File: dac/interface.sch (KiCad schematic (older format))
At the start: 14 parts, among them U17 DS90LV048, U18 74AUP1G74, U19 74AUP1G74

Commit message: DAC board is routed.  I also changed the digital interface to use a buffer (like I did on the input board) so that everything is buffered and we don't have multi-drop nets.
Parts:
- removed C73, C74: 220pF, Capacitor_SMD:C_0603_1608Metric, symbol Device:C_Small
- removed R65, R66: 68, Resistor_SMD:R_0603_1608Metric, symbol Device:R_US
- added C6, C7: 100nF, Capacitor_SMD:C_0603_1608Metric, symbol Device:C_Small
- added RN1, RN2, RN3: 33, Resistor_SMD:R_Array_Convex_4x0603, symbol Device:R_Pack04
- added U2: 74LVC541A, input:my-SSOP-20_5.3x7.2mm_P0.65mm, symbol 74xx:74LS541
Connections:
- net BCK: now also U2.3 (A1), U2.7 (A5)
- net DATA1: now also RN3.7 (R2.2); no longer U17.14 (RO2)
- net DATA2: now also RN3.8 (R1.2); no longer U17.15 (RO1)
- net GND: now also C6.2, C7.2, U2.1 (G1), U2.10 (GND), U2.19 (G2)
- net VCC: now also C6.1, C7.1, U2.20 (VCC)
- net U18FB: now reaches U18.2 (D), U18.3 (~Q)
- net U18Q: now reaches U18.5 (Q), U19.1 (C)
- net U19FB: now reaches U19.2 (D), U19.3 (~Q)
- net DOUT1+ renamed BCK+
- net DOUT1- renamed BCK-
- net DOUT2+ renamed DATA1+
- net DOUT2- renamed DATA1-
- net DOUT3+ renamed DATA2+
- net DOUT3- renamed DATA2-
- net SCK renamed SCK_DRV
- net SCK_DRV: now also U2.4 (A2), U2.8 (A6)
- new net: RN2.1 (R1.1), U2.14 (Y4)
- new net: RN2.2 (R2.1), U2.13 (Y5)
- new net: RN2.3 (R3.1), U2.12 (Y6)
- new net: RN2.4 (R4.1), U2.11 (Y7)
- new net: RN1.1 (R1.1), U2.18 (Y0)
- new net: RN1.2 (R2.1), U2.17 (Y1)
- new net: RN1.3 (R3.1), U2.16 (Y2)
- new net: RN1.4 (R4.1), U2.15 (Y3)
- new net BCK1: RN2.7 (R2.2)
- new net BCK2: RN1.7 (R2.2)
- new net DATA1_DRV: RN3.2 (R2.1), U17.14 (RO2)
- new net DATA2_DRV: RN3.1 (R1.1), U17.15 (RO1)
- new net LRCK1: RN2.8 (R1.2)
- new net LRCK2: RN1.8 (R1.2)
- new net LRCK_IN: U2.2 (A0), U2.6 (A4)
- new net SCK1: RN2.6 (R3.2)
- new net SCK2: RN1.6 (R3.2)
- new net ~RST1: RN2.5 (R4.2)
- new net ~RST2: RN1.5 (R4.2)
- new net ~RST_IN: U2.5 (A3), U2.9 (A7)
- no-connect marks 0 -> 4
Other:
- note added: "DAC serial data in"
- note removed: "Data for DAC 1"
- note removed: "Data for DAC 2"
- moved on the sheet: C75, C76, C77, R61, R62, R63, R64, U17, U18, U19

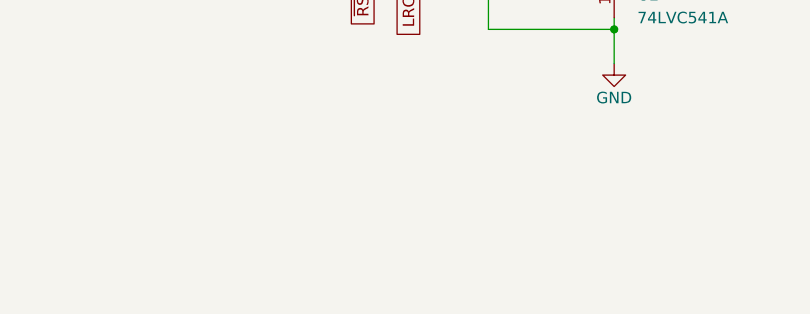
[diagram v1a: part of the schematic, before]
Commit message: Everything seems ready to go for the DAC board.  Made my BOM and checked it twice. Checked footprints of new components and fixed J5, R7-R10.
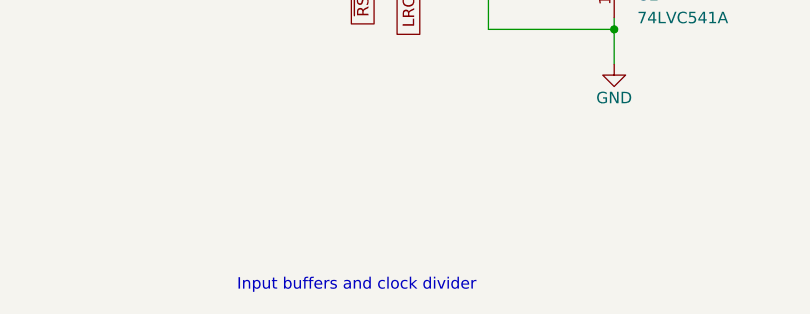
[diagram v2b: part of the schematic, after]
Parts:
- C6, C7: DK line 2 -> I.2
- C75, C76, C77: DK line 18 -> I.2
- R61, R62, R63, R64: DK line 29 -> M.29
- RN1, RN2, RN3: DK line 13 -> I.13
- U17: DK line 26 -> I.39
- U18, U19: DK line 3 -> M.3
- U2: DK line 11 -> I.11
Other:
- note added: "Input buffers and clock divider"
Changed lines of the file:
@@
 F 2 "Package_SO:TSSOP-16_4.4x5mm_P0.65mm" H 3100 800 50  0001 C CNN
 F 3 "http://www.ti.com/general/docs/suppproductinfo.tsp?distId=10&gotoUrl=http%3A%2F%2Fwww.ti.com%2Flit%2Fgpn%2Fds90lv048a" H 2400 1700 50  0001 C CNN
-F 4 "26" H 3100 2550 50  0001 C CNN "DK line"
+F 4 "I.39" H 3100 2550 50  0001 C CNN "DK line"
 F 5 "0/4 Receiver  LVDS 16-TSSOP" H 3100 2550 50  0001 C CNN "Description"
 F 6 "DS90LV048ATMTC/NOPB-ND" H 3100 2550 50  0001 C CNN "Digikey"
@@
 F 3 "https://www.seielect.com/catalog/sei-rncp.pdf" H 1950 2750 50  0001 C CNN
 F 4 "RNCP0603FTD100RCT-ND" H 1950 2750 50  0001 C CNN "Digikey"
-F 5 "29" H 1950 2750 50  0001 C CNN "DK line"
+F 5 "M.29" H 1950 2750 50  0001 C CNN "DK line"
 F 6 "RES 100 OHM 1% 1/8W 0603" H 1950 2750 50  0001 C CNN "Description"
 F 7 "RNCP0603FTD100R" H 1950 2750 50  0001 C CNN "MPN"
@@
 F 3 "https://www.seielect.com/catalog/sei-rncp.pdf" H 1950 3150 50  0001 C CNN
 F 4 "RNCP0603FTD100RCT-ND" H 1950 3150 50  0001 C CNN "Digikey"
-F 5 "29" H 1950 3150 50  0001 C CNN "DK line"
+F 5 "M.29" H 1950 3150 50  0001 C CNN "DK line"
 F 6 "RES 100 OHM 1% 1/8W 0603" H 1950 3150 50  0001 C CNN "Description"
 F 7 "RNCP0603FTD100R" H 1950 3150 50  0001 C CNN "MPN"
@@
 F 3 "https://www.seielect.com/catalog/sei-rncp.pdf" H 1950 3550 50  0001 C CNN
 F 4 "RNCP0603FTD100RCT-ND" H 1950 3550 50  0001 C CNN "Digikey"
-F 5 "29" H 1950 3550 50  0001 C CNN "DK line"
+F 5 "M.29" H 1950 3550 50  0001 C CNN "DK line"
 F 6 "RES 100 OHM 1% 1/8W 0603" H 1950 3550 50  0001 C CNN "Description"
 F 7 "RNCP0603FTD100R" H 1950 3550 50  0001 C CNN "MPN"
@@
 F 4 "CAP CER 0.1UF 25V X7R 0603" H 2850 1800 50  0001 C CNN "Description"
 F 5 "311-1341-1-ND" H 2850 1800 50  0001 C CNN "Digikey"
-F 6 "18" H 2850 1800 50  0001 C CNN "DK line"
+F 6 "I.2" H 2850 1800 50  0001 C CNN "DK line"
 F 7 "" H 2850 1800 50  0001 C CNN "MFG"
 F 8 "CC0603KRX7R8BB104" H 2850 1800 50  0001 C CNN "MPN"
@@
 F 3 "https://www.seielect.com/catalog/sei-rncp.pdf" H 1950 2350 50  0001 C CNN
 F 4 "RNCP0603FTD100RCT-ND" H 1950 2350 50  0001 C CNN "Digikey"
-F 5 "29" H 1950 2350 50  0001 C CNN "DK line"
+F 5 "M.29" H 1950 2350 50  0001 C CNN "DK line"
 F 6 "RES 100 OHM 1% 1/8W 0603" H 1950 2350 50  0001 C CNN "Description"
 F 7 "RNCP0603FTD100R" H 1950 2350 50  0001 C CNN "MPN"
@@
 F 4 "CAP CER 0.1UF 25V X7R 0603" H 5350 3050 50  0001 C CNN "Description"
 F 5 "311-1341-1-ND" H 5350 3050 50  0001 C CNN "Digikey"
-F 6 "18" H 5350 3050 50  0001 C CNN "DK line"
+F 6 "I.2" H 5350 3050 50  0001 C CNN "DK line"
 F 7 "" H 5350 3050 50  0001 C CNN "MFG"
 F 8 "CC0603KRX7R8BB104" H 5350 3050 50  0001 C CNN "MPN"
@@
 F 4 "CAP CER 0.1UF 25V X7R 0603" H 6450 3050 50  0001 C CNN "Description"
 F 5 "311-1341-1-ND" H 6450 3050 50  0001 C CNN "Digikey"
-F 6 "18" H 6450 3050 50  0001 C CNN "DK line"
+F 6 "I.2" H 6450 3050 50  0001 C CNN "DK line"
 F 7 "" H 6450 3050 50  0001 C CNN "MFG"
 F 8 "CC0603KRX7R8BB104" H 6450 3050 50  0001 C CNN "MPN"
@@
 F 7 "IC FF D-TYPE SNGL 1BIT 8VSSOP" H 6150 3450 50  0001 C CNN "Description"
 F 8 "Nexperia USA Inc." H 6150 3450 50  0001 C CNN "Manufacturer"
-F 9 "3" H 6150 3450 50  0001 C CNN "DK line"
+F 9 "M.3" H 6150 3450 50  0001 C CNN "DK line"
 	1    6150 3450
 	1    0    0    -1
@@
 F 7 "IC FF D-TYPE SNGL 1BIT 8VSSOP" H 5050 3450 50  0001 C CNN "Description"
 F 8 "Nexperia USA Inc." H 5050 3450 50  0001 C CNN "Manufacturer"
-F 9 "3" H 5050 3450 50  0001 C CNN "DK line"
+F 9 "M.3" H 5050 3450 50  0001 C CNN "DK line"
 	1    5050 3450
 	1    0    0    -1
@@
 F 2 "Resistor_SMD:R_Array_Convex_4x0603" V 9975 4950 50  0001 C CNN
 F 3 "https://www.bourns.com/docs/Product-Datasheets/CATCAY.pdf" H 9700 4950 50  0001 C CNN
-F 4 "13" H 9700 4950 50  0001 C CNN "DK line"
+F 4 "I.13" H 9700 4950 50  0001 C CNN "DK line"
 F 5 "RES ARRAY 4 RES 33 OHM 1206" H 9700 4950 50  0001 C CNN "Description"
 F 6 "CAY16-330J4LFCT-ND" H 9700 4950 50  0001 C CNN "Digikey"
@@
 F 2 "Resistor_SMD:R_Array_Convex_4x0603" V 9975 4500 50  0001 C CNN
 F 3 "https://www.bourns.com/docs/Product-Datasheets/CATCAY.pdf" H 9700 4500 50  0001 C CNN
-F 4 "13" H 9700 4500 50  0001 C CNN "DK line"
+F 4 "I.13" H 9700 4500 50  0001 C CNN "DK line"
 F 5 "RES ARRAY 4 RES 33 OHM 1206" H 9700 4500 50  0001 C CNN "Description"
 F 6 "CAY16-330J4LFCT-ND" H 9700 4500 50  0001 C CNN "Digikey"
@@
 F 1 "100nF" V 8425 3750 50  0000 L CNN
 F 2 "Capacitor_SMD:C_0603_1608Metric" H 8550 3850 50  0001 C CNN
-F 3 "~" H 8550 3850 50  0001 C CNN
+F 3 "https://www.yageo.com/upload/media/product/productsearch/datasheet/mlcc/UPY-GPHC_X7R_6.3V-to-50V_18.pdf" H 8550 3850 50  0001 C CNN
 F 4 "CAP CER 0.1UF 25V X7R 0603" H 8550 3850 50  0001 C CNN "Description"
 F 5 "311-1341-1-ND" H 8550 3850 50  0001 C CNN "Digikey"
-F 6 "2" H 8550 3850 50  0001 C CNN "DK line"
+F 6 "I.2" H 8550 3850 50  0001 C CNN "DK line"
 F 7 "CC0603KRX7R8BB104" H 8550 3850 50  0001 C CNN "MPN"
 F 8 "Yageo" H 8550 3850 50  0001 C CNN "Manufacturer"
@@
 F 1 "100nF" V 9175 3725 50  0000 L CNN
 F 2 "Capacitor_SMD:C_0603_1608Metric" H 9050 3850 50  0001 C CNN
-F 3 "~" H 9050 3850 50  0001 C CNN
+F 3 "https://www.yageo.com/upload/media/product/productsearch/datasheet/mlcc/UPY-GPHC_X7R_6.3V-to-50V_18.pdf" H 9050 3850 50  0001 C CNN
 F 4 "CAP CER 0.1UF 25V X7R 0603" H 9050 3850 50  0001 C CNN "Description"
 F 5 "311-1341-1-ND" H 9050 3850 50  0001 C CNN "Digikey"
-F 6 "2" H 9050 3850 50  0001 C CNN "DK line"
+F 6 "I.2" H 9050 3850 50  0001 C CNN "DK line"
 F 7 "CC0603KRX7R8BB104" H 9050 3850 50  0001 C CNN "MPN"
 F 8 "Yageo" H 9050 3850 50  0001 C CNN "Manufacturer"
@@
 F 2 "input:my-SSOP-20_5.3x7.2mm_P0.65mm" H 8800 4800 50  0001 C CNN
 F 3 "http://www.ti.com/lit/gpn/sn74LS541" H 8800 4800 50  0001 C CNN
-F 4 "11" H 8800 4800 50  0001 C CNN "DK line"
+F 4 "I.11" H 8800 4800 50  0001 C CNN "DK line"
 F 5 "IC BUF NON-INVERT 3.6V 20SSOP" H 8800 4800 50  0001 C CNN "Description"
 F 6 "296-8518-1-ND" H 8800 4800 50  0001 C CNN "Digikey"
@@
 F 2 "Resistor_SMD:R_Array_Convex_4x0603" V 5175 2400 50  0001 C CNN
 F 3 "https://www.bourns.com/docs/Product-Datasheets/CATCAY.pdf" H 4900 2400 50  0001 C CNN
-F 4 "13" H 4900 2400 50  0001 C CNN "DK line"
+F 4 "I.13" H 4900 2400 50  0001 C CNN "DK line"
 F 5 "RES ARRAY 4 RES 33 OHM 1206" H 4900 2400 50  0001 C CNN "Description"
 F 6 "CAY16-330J4LFCT-ND" H 4900 2400 50  0001 C CNN "Digikey"
@@
 Wire Wire Line
 	3600 2750 4500 2750
+Text Notes 7150 6800 0    50   ~ 0
+Input buffers and clock divider
 $EndSCHEMATC
